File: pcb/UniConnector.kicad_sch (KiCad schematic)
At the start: 1 part

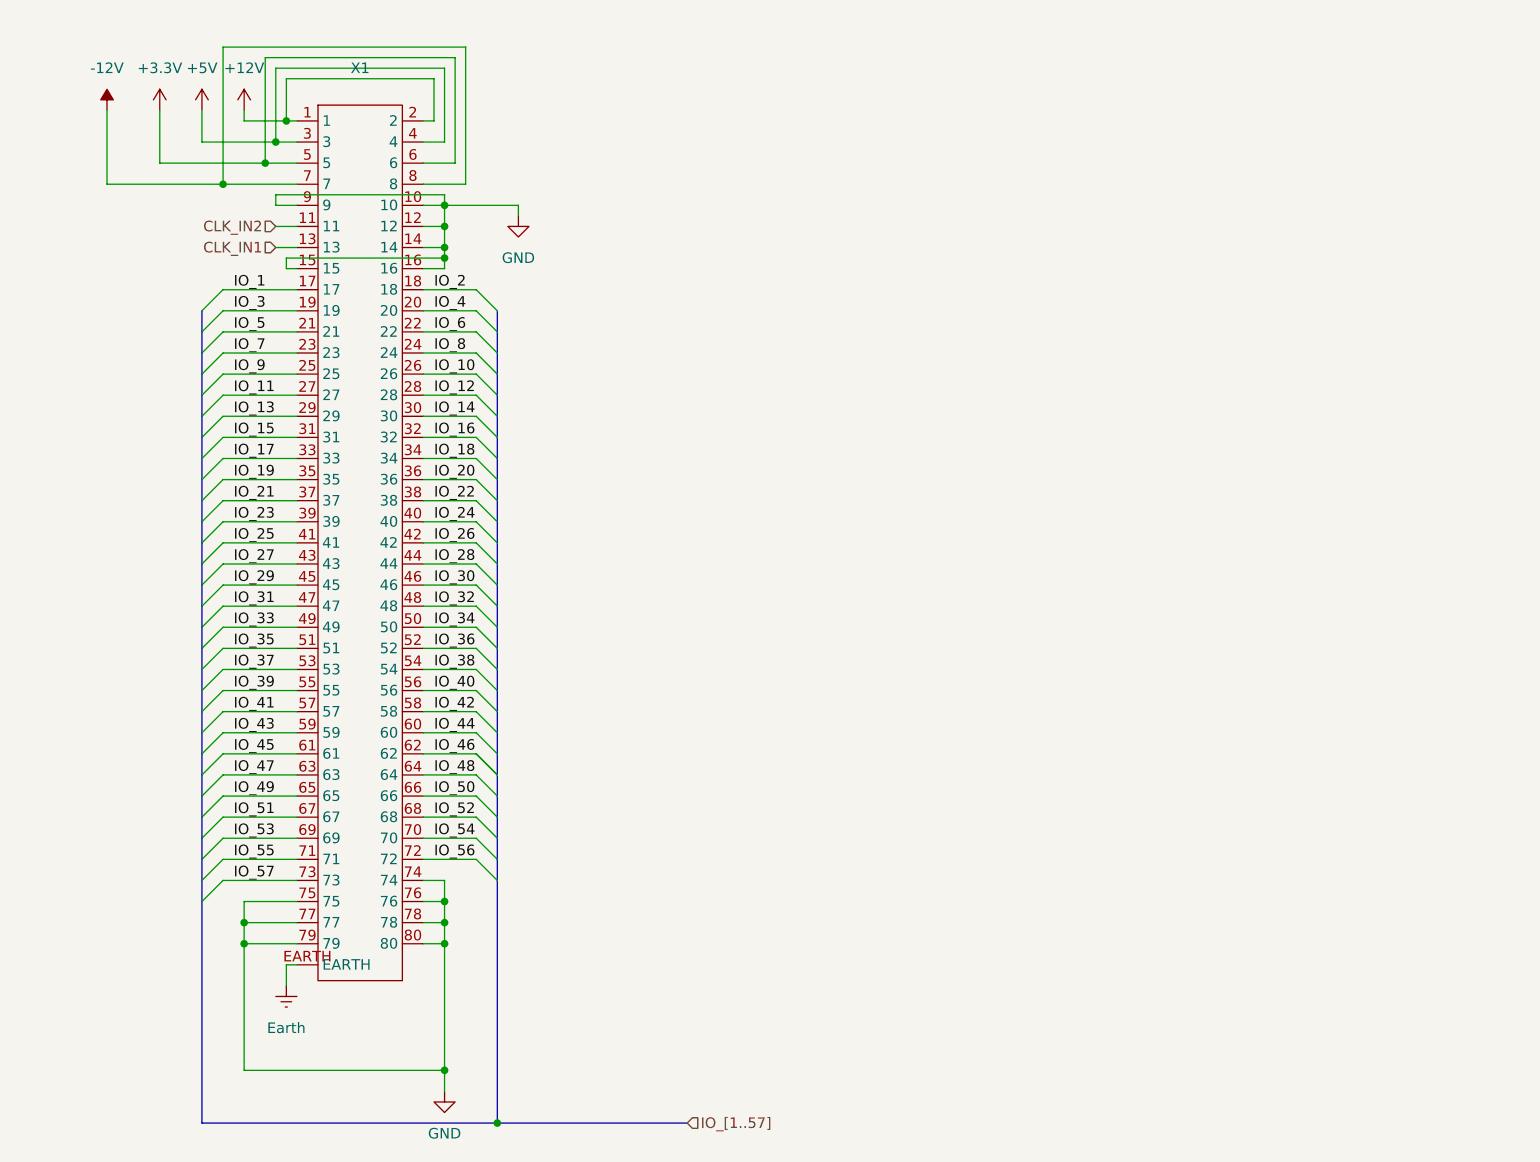
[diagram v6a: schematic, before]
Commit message: Added ESD protection to UniConnector, more routing and polishing
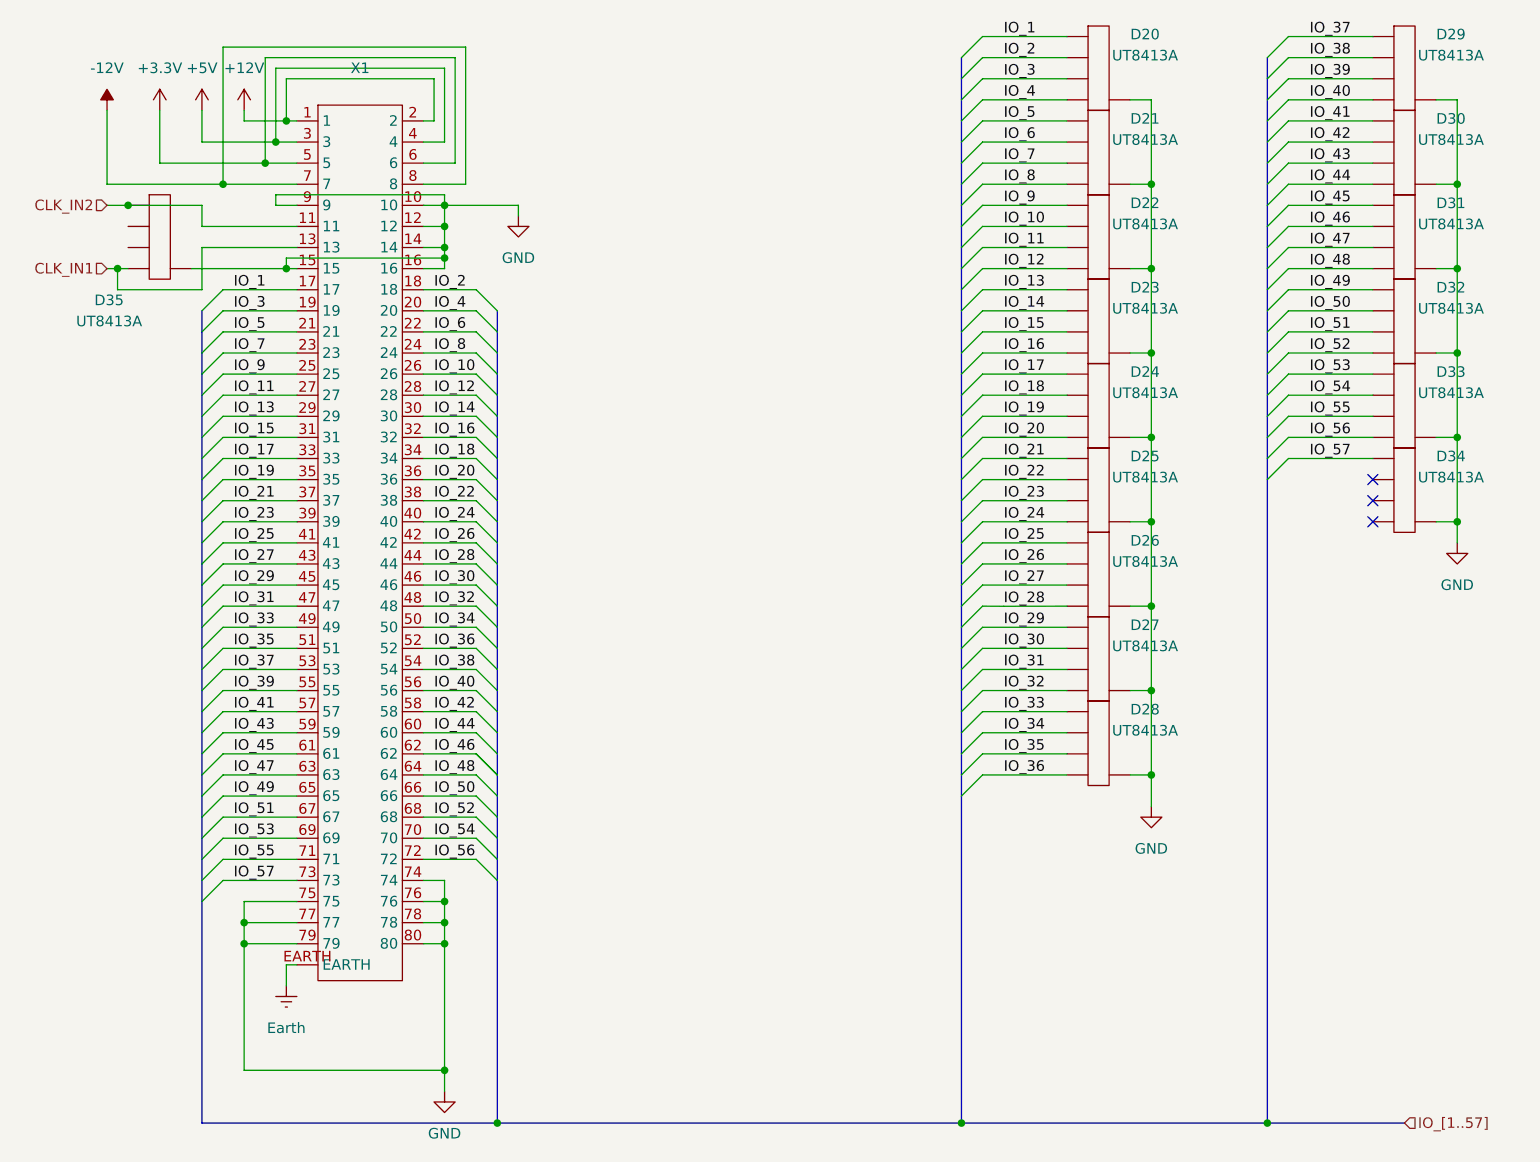
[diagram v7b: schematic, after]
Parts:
- added D20, D21, D22, D23, D24, D25, D26, D27, D28, D29, D30, D31, D32, D33, D34, D35: UT8413A, Package_DFN_QFN:Diodes_UDFN-10_1.0x2.5mm_P0.5mm, symbol Conn:UT8413A
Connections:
- net CLK_IN1: now also D35.1, D35.10
- net CLK_IN2: now also D35.5, D35.6
- net GND: now also D20.3, D20.8, D21.3, D21.8, D22.3, D22.8, D23.3, D23.8, D24.3, D24.8, D25.3, D25.8, D26.3, D26.8, D27.3, D27.8, D28.3, D28.8, D29.3, D29.8, D30.3, D30.8, D31.3, D31.8, D32.3, D32.8, D33.3, D33.8, D34.3, D34.8, D35.3, D35.8
- net IO_1: now also D20.5, D20.6
- net IO_10: now also D22.4, D22.7
- net IO_11: now also D22.2, D22.9
- net IO_12: now also D22.1, D22.10
- net IO_13: now also D23.5, D23.6
- net IO_14: now also D23.4, D23.7
- net IO_15: now also D23.2, D23.9
- net IO_16: now also D23.1, D23.10
- net IO_17: now also D24.5, D24.6
- net IO_18: now also D24.4, D24.7
- net IO_19: now also D24.2, D24.9
- net IO_2: now also D20.4, D20.7
- net IO_20: now also D24.1, D24.10
- net IO_21: now also D25.5, D25.6
- net IO_22: now also D25.4, D25.7
- net IO_23: now also D25.2, D25.9
- net IO_24: now also D25.1, D25.10
- net IO_25: now also D26.5, D26.6
- net IO_26: now also D26.4, D26.7
- net IO_27: now also D26.2, D26.9
- net IO_28: now also D26.1, D26.10
- net IO_29: now also D27.5, D27.6
- net IO_3: now also D20.2, D20.9
- net IO_30: now also D27.4, D27.7
- net IO_31: now also D27.2, D27.9
- net IO_32: now also D27.1, D27.10
- net IO_33: now also D28.5, D28.6
- net IO_34: now also D28.4, D28.7
- net IO_35: now also D28.2, D28.9
- net IO_36: now also D28.1, D28.10
- net IO_37: now also D29.5, D29.6
- net IO_38: now also D29.4, D29.7
- net IO_39: now also D29.2, D29.9
- net IO_4: now also D20.1, D20.10
- net IO_40: now also D29.1, D29.10
- net IO_41: now also D30.5, D30.6
- net IO_42: now also D30.4, D30.7
- net IO_43: now also D30.2, D30.9
- net IO_44: now also D30.1, D30.10
- net IO_45: now also D31.5, D31.6
- net IO_46: now also D31.4, D31.7
- net IO_47: now also D31.2, D31.9
- net IO_48: now also D31.1, D31.10
- net IO_49: now also D32.5, D32.6
- net IO_5: now also D21.5, D21.6
- net IO_50: now also D32.4, D32.7
- net IO_51: now also D32.2, D32.9
- net IO_52: now also D32.1, D32.10
- net IO_53: now also D33.5, D33.6
- net IO_54: now also D33.4, D33.7
- net IO_55: now also D33.2, D33.9
- net IO_56: now also D33.1, D33.10
- net IO_57: now also D34.5, D34.6
- net IO_6: now also D21.4, D21.7
- net IO_7: now also D21.2, D21.9
- net IO_8: now also D21.1, D21.10
- net IO_9: now also D22.5, D22.6
- new net: D34.1, D34.10
- new net: D34.2, D34.9
- new net: D34.4, D34.7
- new net: D35.2, D35.9
- new net: D35.4, D35.7
- no-connect marks 0 -> 3
